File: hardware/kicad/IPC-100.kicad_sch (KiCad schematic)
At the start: 0 parts

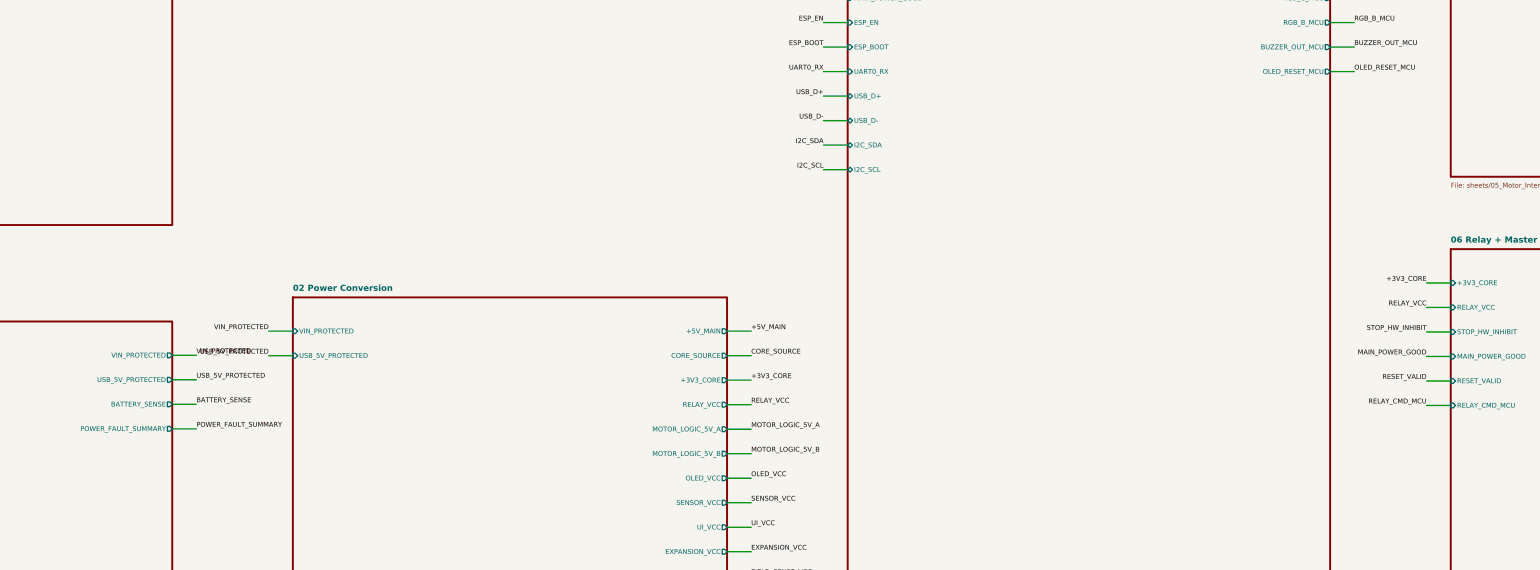
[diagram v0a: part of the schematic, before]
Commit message: Resolve Rev A power control interfaces
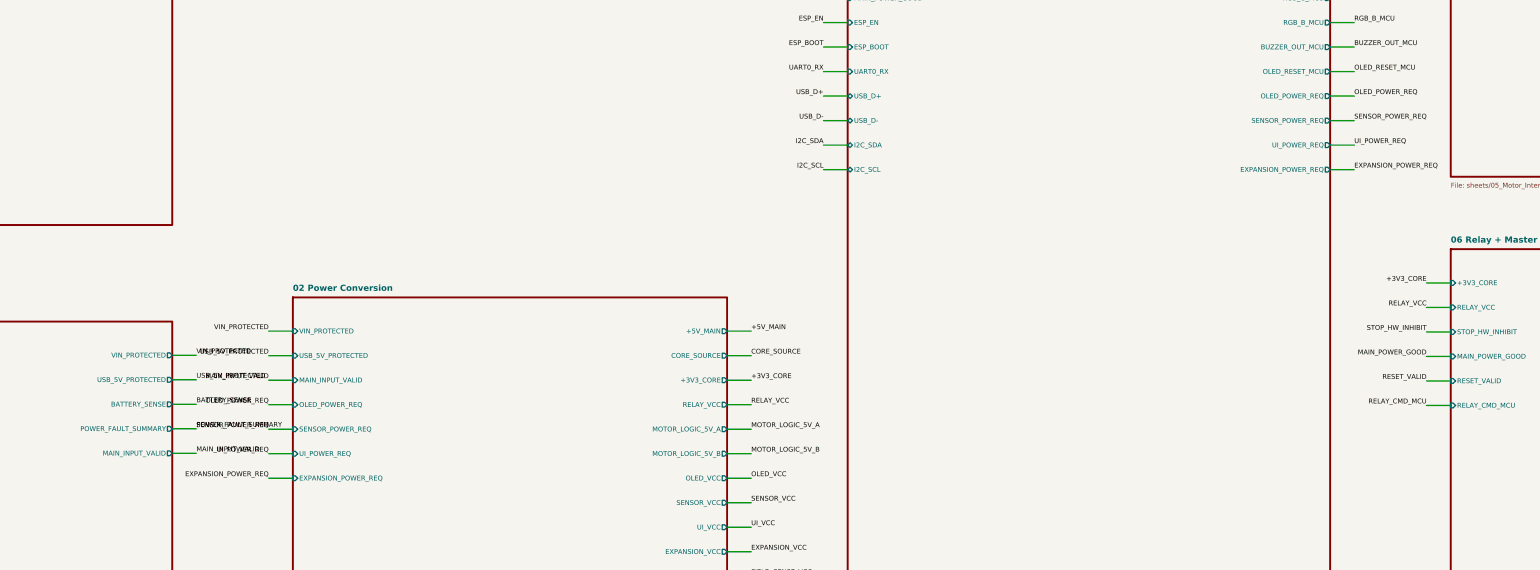
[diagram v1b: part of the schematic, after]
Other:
- sheet 01 Power Entry & Protection ports: added MAIN_INPUT_VALID; removed none
- sheet 02 Power Conversion ports: added EXPANSION_POWER_REQ, MAIN_INPUT_VALID, OLED_POWER_REQ, SENSOR_POWER_REQ, UI_POWER_REQ; removed none
- sheet 03 ESP32 Core ports: added EXPANSION_POWER_REQ, OLED_POWER_REQ, SENSOR_POWER_REQ, UI_POWER_REQ; removed none
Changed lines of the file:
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@@
+      (effects (font (size 1.0 1.0)) (justify right))
+    )
+    (pin "MAIN_INPUT_VALID" output (at 110 237.32 0)
       (effects (font (size 1.0 1.0)) (justify right))
     )
@@
   )
   (label "POWER_FAULT_SUMMARY" (at 115 232.24 0)
+    (effects (font (size 1.0 1.0)) (justify left bottom))
+  )
+  (wire (pts (xy 110 237.32) (xy 115 237.32))
+    (stroke (width 0) (type default))
+  )
+  (label "MAIN_INPUT_VALID" (at 115 237.32 0)
     (effects (font (size 1.0 1.0)) (justify left bottom))
   )
@@
       (effects (font (size 1.0 1.0)) (justify left))
     )
+    (pin "MAIN_INPUT_VALID" input (at 135 222.16 180)
+      (effects (font (size 1.0 1.0)) (justify left))
+    )
+    (pin "OLED_POWER_REQ" input (at 135 227.24 180)
+      (effects (font (size 1.0 1.0)) (justify left))
+    )
+    (pin "SENSOR_POWER_REQ" input (at 135 232.32 180)
+      (effects (font (size 1.0 1.0)) (justify left))
+    )
+    (pin "UI_POWER_REQ" input (at 135 237.40 180)
+      (effects (font (size 1.0 1.0)) (justify left))
+    )
+    (pin "EXPANSION_POWER_REQ" input (at 135 242.48 180)
+      (effects (font (size 1.0 1.0)) (justify left))
+    )
     (pin "+5V_MAIN" output (at 225 212.00 0)
       (effects (font (size 1.0 1.0)) (justify right))
@@
   )
   (label "USB_5V_PROTECTED" (at 130 217.08 180)
+    (effects (font (size 1.0 1.0)) (justify right bottom))
+  )
+  (wire (pts (xy 135 222.16) (xy 130 222.16))
+    (stroke (width 0) (type default))
+  )
+  (label "MAIN_INPUT_VALID" (at 130 222.16 180)
+    (effects (font (size 1.0 1.0)) (justify right bottom))
+  )
+  (wire (pts (xy 135 227.24) (xy 130 227.24))
+    (stroke (width 0) (type default))
+  )
+  (label "OLED_POWER_REQ" (at 130 227.24 180)
+    (effects (font (size 1.0 1.0)) (justify right bottom))
+  )
+  (wire (pts (xy 135 232.32) (xy 130 232.32))
+    (stroke (width 0) (type default))
+  )
+  (label "SENSOR_POWER_REQ" (at 130 232.32 180)
+    (effects (font (size 1.0 1.0)) (justify right bottom))
+  )
+  (wire (pts (xy 135 237.40) (xy 130 237.40))
+    (stroke (width 0) (type default))
+  )
+  (label "UI_POWER_REQ" (at 130 237.40 180)
+    (effects (font (size 1.0 1.0)) (justify right bottom))
+  )
+  (wire (pts (xy 135 242.48) (xy 130 242.48))
+    (stroke (width 0) (type default))
+  )
+  (label "EXPANSION_POWER_REQ" (at 130 242.48 180)
     (effects (font (size 1.0 1.0)) (justify right bottom))
   )
@@
       (effects (font (size 1.0 1.0)) (justify right))
     )
+    (pin "OLED_POWER_REQ" output (at 350 163.28 0)
+      (effects (font (size 1.0 1.0)) (justify right))
+    )
+    (pin "SENSOR_POWER_REQ" output (at 350 168.36 0)
+      (effects (font (size 1.0 1.0)) (justify right))
+    )
+    (pin "UI_POWER_REQ" output (at 350 173.44 0)
+      (effects (font (size 1.0 1.0)) (justify right))
+    )
+    (pin "EXPANSION_POWER_REQ" output (at 350 178.52 0)
+      (effects (font (size 1.0 1.0)) (justify right))
+    )
     (instances
       (project "IPC-100"
@@
     (effects (font (size 1.0 1.0)) (justify left bottom))
   )
+  (wire (pts (xy 350 163.28) (xy 355 163.28))
+    (stroke (width 0) (type default))
+  )
+  (label "OLED_POWER_REQ" (at 355 163.28 0)
+    (effects (font (size 1.0 1.0)) (justify left bottom))
+  )
+  (wire (pts (xy 350 168.36) (xy 355 168.36))
+    (stroke (width 0) (type default))
+  )
+  (label "SENSOR_POWER_REQ" (at 355 168.36 0)
+    (effects (font (size 1.0 1.0)) (justify left bottom))
+  )
+  (wire (pts (xy 350 173.44) (xy 355 173.44))
+    (stroke (width 0) (type default))
+  )
+  (label "UI_POWER_REQ" (at 355 173.44 0)
+    (effects (font (size 1.0 1.0)) (justify left bottom))
+  )
+  (wire (pts (xy 350 178.52) (xy 355 178.52))
+    (stroke (width 0) (type default))
+  )
+  (label "EXPANSION_POWER_REQ" (at 355 178.52 0)
+    (effects (font (size 1.0 1.0)) (justify left bottom))
+  )

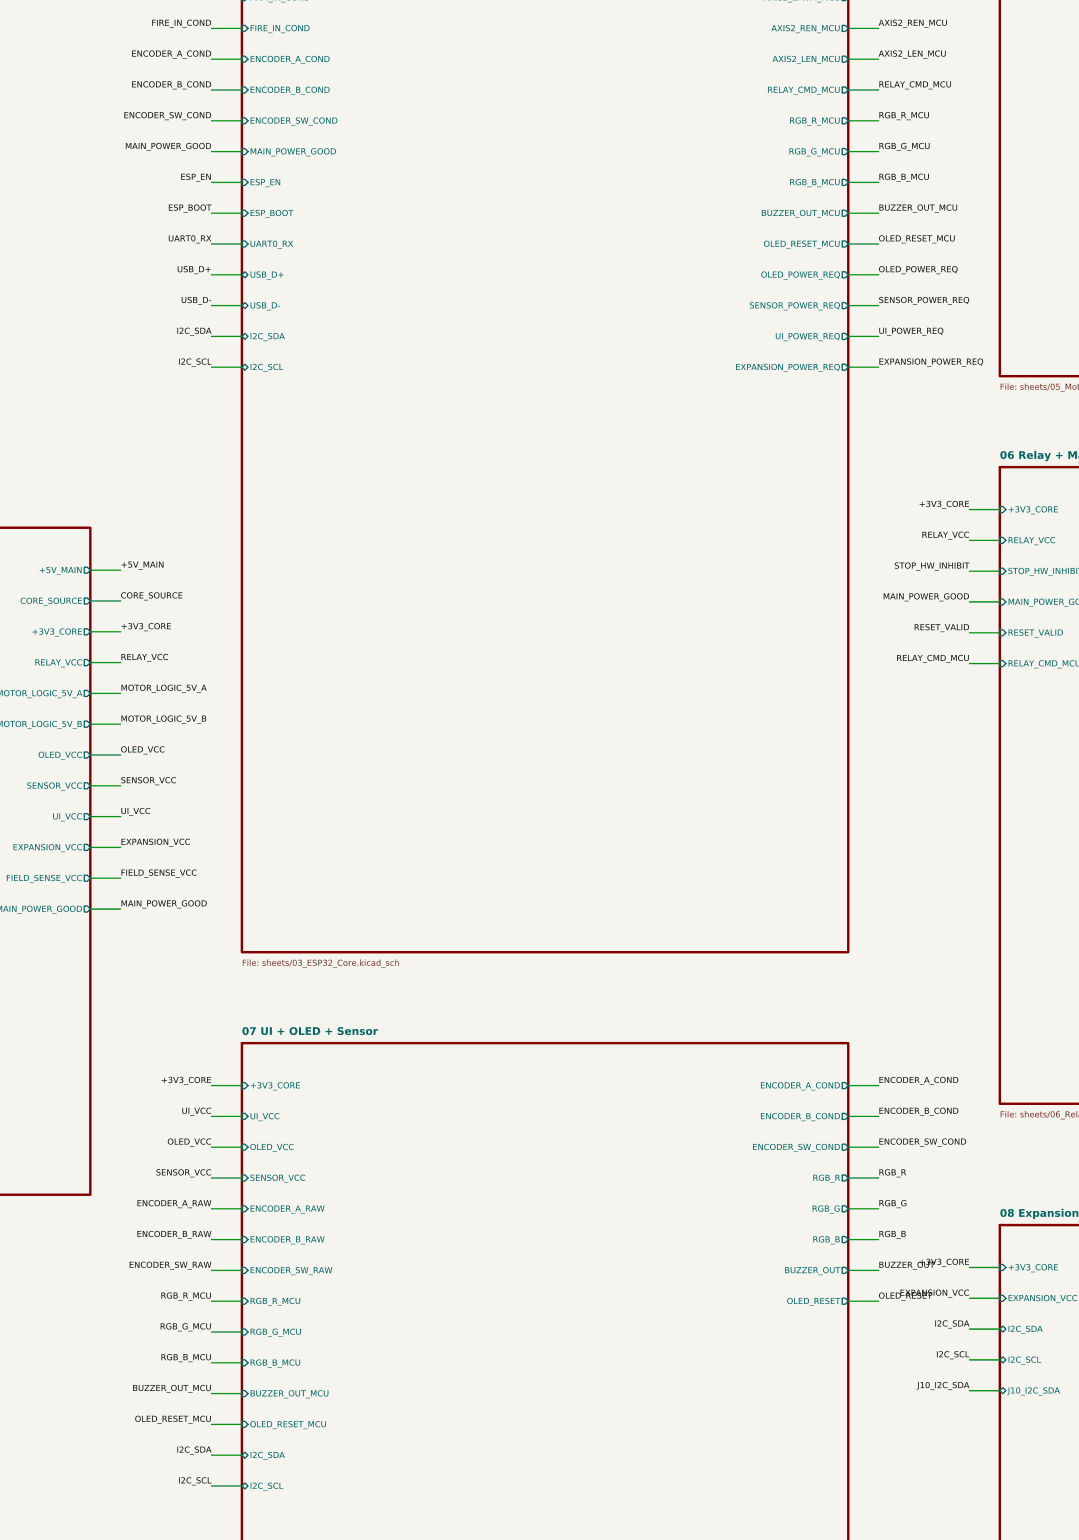
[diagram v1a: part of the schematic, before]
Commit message: Implement ESP32-S3 core subsystem
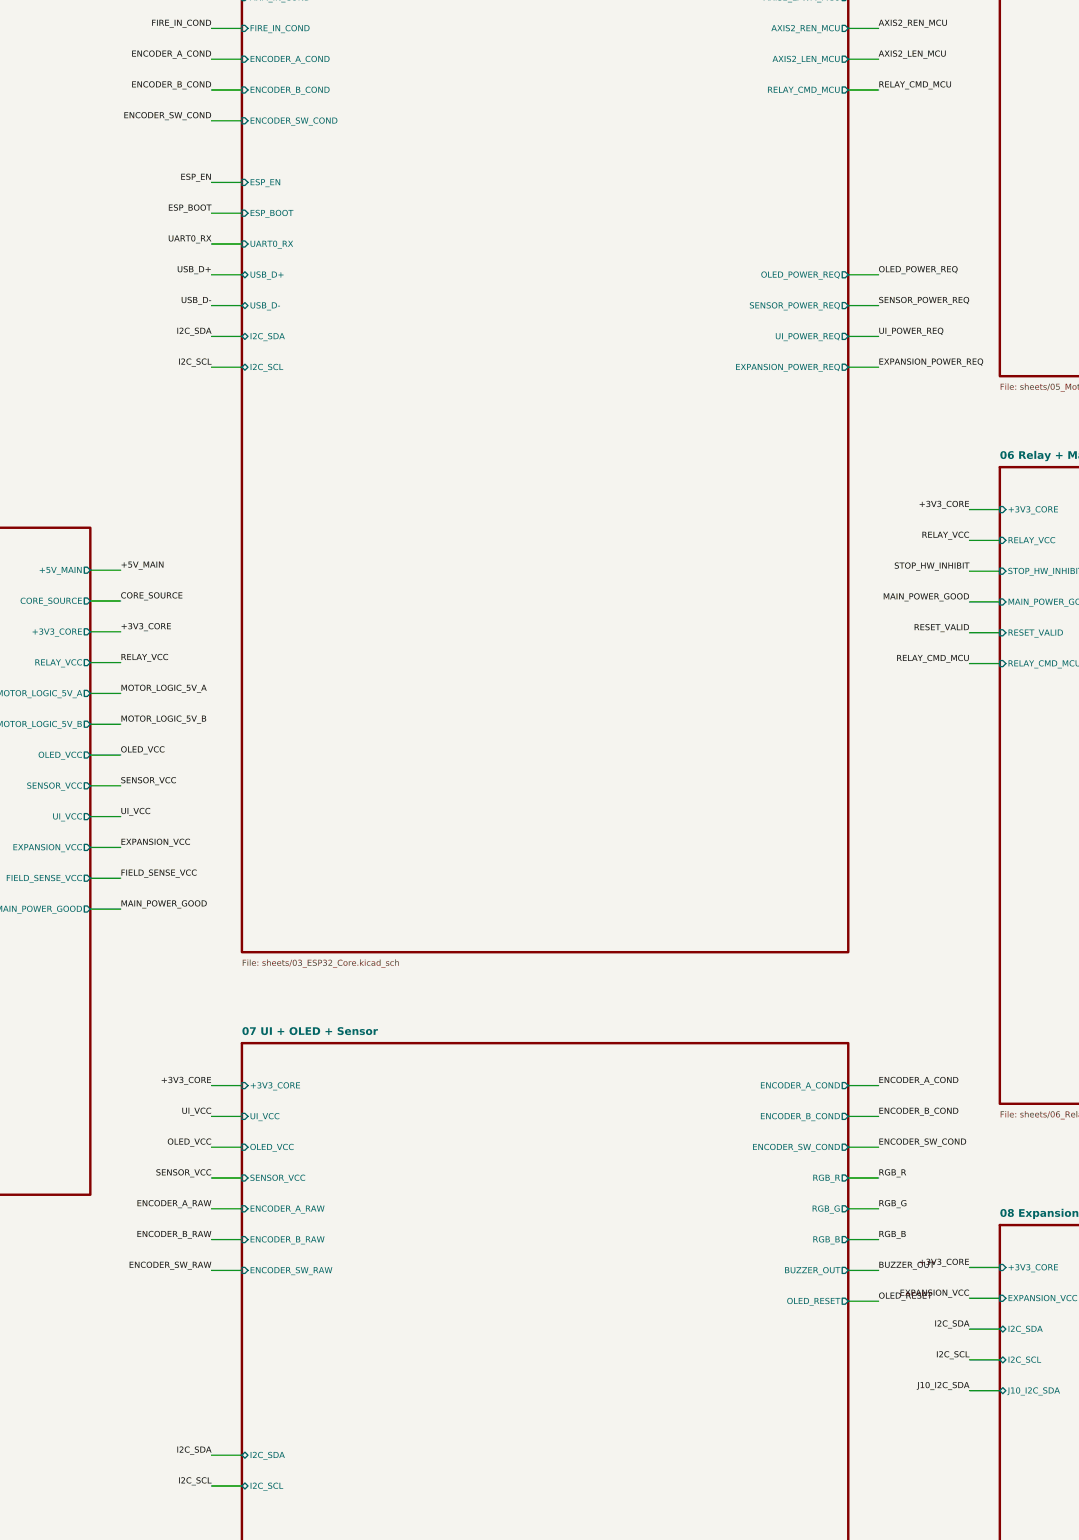
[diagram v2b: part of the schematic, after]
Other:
- sheet 03 ESP32 Core ports: added none; removed BUZZER_OUT_MCU, MAIN_POWER_GOOD, OLED_RESET_MCU, RGB_B_MCU, RGB_G_MCU, RGB_R_MCU
- sheet 07 UI + OLED + Sensor ports: added none; removed BUZZER_OUT_MCU, OLED_RESET_MCU, RGB_B_MCU, RGB_G_MCU, RGB_R_MCU
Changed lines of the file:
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@@
-      (effects (font (size 1.0 1.0)) (justify left))
-    )
-    (pin "MAIN_POWER_GOOD" input (at 250 142.96 180)
       (effects (font (size 1.0 1.0)) (justify left))
     )
@@
     )
     (pin "RELAY_CMD_MCU" output (at 350 132.80 0)
-      (effects (font (size 1.0 1.0)) (justify right))
-    )
-    (pin "RGB_R_MCU" output (at 350 137.88 0)
-      (effects (font (size 1.0 1.0)) (justify right))
-    )
-    (pin "RGB_G_MCU" output (at 350 142.96 0)
-      (effects (font (size 1.0 1.0)) (justify right))
-    )
-    (pin "RGB_B_MCU" output (at 350 148.04 0)
-      (effects (font (size 1.0 1.0)) (justify right))
-    )
-    (pin "BUZZER_OUT_MCU" output (at 350 153.12 0)
-      (effects (font (size 1.0 1.0)) (justify right))
-    )
-    (pin "OLED_RESET_MCU" output (at 350 158.20 0)
       (effects (font (size 1.0 1.0)) (justify right))
     )
@@
     (effects (font (size 1.0 1.0)) (justify right bottom))
   )
-  (wire (pts (xy 250 142.96) (xy 245 142.96))
-    (stroke (width 0) (type default))
-  )
-  (label "MAIN_POWER_GOOD" (at 245 142.96 180)
-    (effects (font (size 1.0 1.0)) (justify right bottom))
-  )
   (wire (pts (xy 250 148.04) (xy 245 148.04))
     (stroke (width 0) (type default))
@@
   )
   (label "RELAY_CMD_MCU" (at 355 132.80 0)
-    (effects (font (size 1.0 1.0)) (justify left bottom))
-  )
-  (wire (pts (xy 350 137.88) (xy 355 137.88))
-    (stroke (width 0) (type default))
-  )
-  (label "RGB_R_MCU" (at 355 137.88 0)
-    (effects (font (size 1.0 1.0)) (justify left bottom))
-  )
-  (wire (pts (xy 350 142.96) (xy 355 142.96))
-    (stroke (width 0) (type default))
-  )
-  (label "RGB_G_MCU" (at 355 142.96 0)
-    (effects (font (size 1.0 1.0)) (justify left bottom))
-  )
-  (wire (pts (xy 350 148.04) (xy 355 148.04))
-    (stroke (width 0) (type default))
-  )
-  (label "RGB_B_MCU" (at 355 148.04 0)
-    (effects (font (size 1.0 1.0)) (justify left bottom))
-  )
-  (wire (pts (xy 350 153.12) (xy 355 153.12))
-    (stroke (width 0) (type default))
-  )
-  (label "BUZZER_OUT_MCU" (at 355 153.12 0)
-    (effects (font (size 1.0 1.0)) (justify left bottom))
-  )
-  (wire (pts (xy 350 158.20) (xy 355 158.20))
-    (stroke (width 0) (type default))
-  )
-  (label "OLED_RESET_MCU" (at 355 158.20 0)
     (effects (font (size 1.0 1.0)) (justify left bottom))
   )
@@
       (effects (font (size 1.0 1.0)) (justify left))
     )
-    (pin "RGB_R_MCU" input (at 250 332.56 180)
-      (effects (font (size 1.0 1.0)) (justify left))
-    )
-    (pin "RGB_G_MCU" input (at 250 337.64 180)
-      (effects (font (size 1.0 1.0)) (justify left))
-    )
-    (pin "RGB_B_MCU" input (at 250 342.72 180)
-      (effects (font (size 1.0 1.0)) (justify left))
-    )
-    (pin "BUZZER_OUT_MCU" input (at 250 347.80 180)
-      (effects (font (size 1.0 1.0)) (justify left))
-    )
-    (pin "OLED_RESET_MCU" input (at 250 352.88 180)
-      (effects (font (size 1.0 1.0)) (justify left))
-    )
     (pin "I2C_SDA" bidirectional (at 250 357.96 180)
       (effects (font (size 1.0 1.0)) (justify left))
@@
     (effects (font (size 1.0 1.0)) (justify right bottom))
   )
-  (wire (pts (xy 250 332.56) (xy 245 332.56))
-    (stroke (width 0) (type default))
-  )
-  (label "RGB_R_MCU" (at 245 332.56 180)
-    (effects (font (size 1.0 1.0)) (justify right bottom))
-  )
-  (wire (pts (xy 250 337.64) (xy 245 337.64))
-    (stroke (width 0) (type default))
-  )
-  (label "RGB_G_MCU" (at 245 337.64 180)
-    (effects (font (size 1.0 1.0)) (justify right bottom))
-  )
-  (wire (pts (xy 250 342.72) (xy 245 342.72))
-    (stroke (width 0) (type default))
-  )
-  (label "RGB_B_MCU" (at 245 342.72 180)
-    (effects (font (size 1.0 1.0)) (justify right bottom))
-  )
-  (wire (pts (xy 250 347.80) (xy 245 347.80))
-    (stroke (width 0) (type default))
-  )
-  (label "BUZZER_OUT_MCU" (at 245 347.80 180)
-    (effects (font (size 1.0 1.0)) (justify right bottom))
-  )
-  (wire (pts (xy 250 352.88) (xy 245 352.88))
-    (stroke (width 0) (type default))
-  )
-  (label "OLED_RESET_MCU" (at 245 352.88 180)
-    (effects (font (size 1.0 1.0)) (justify right bottom))
-  )
